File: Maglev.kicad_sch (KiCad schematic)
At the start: 25 parts, among them J1 629722000214, J2 691103110002, J3 61300621121, J4 61300821121, U1 WE-TVS-82400102, U2 ESP32-C3

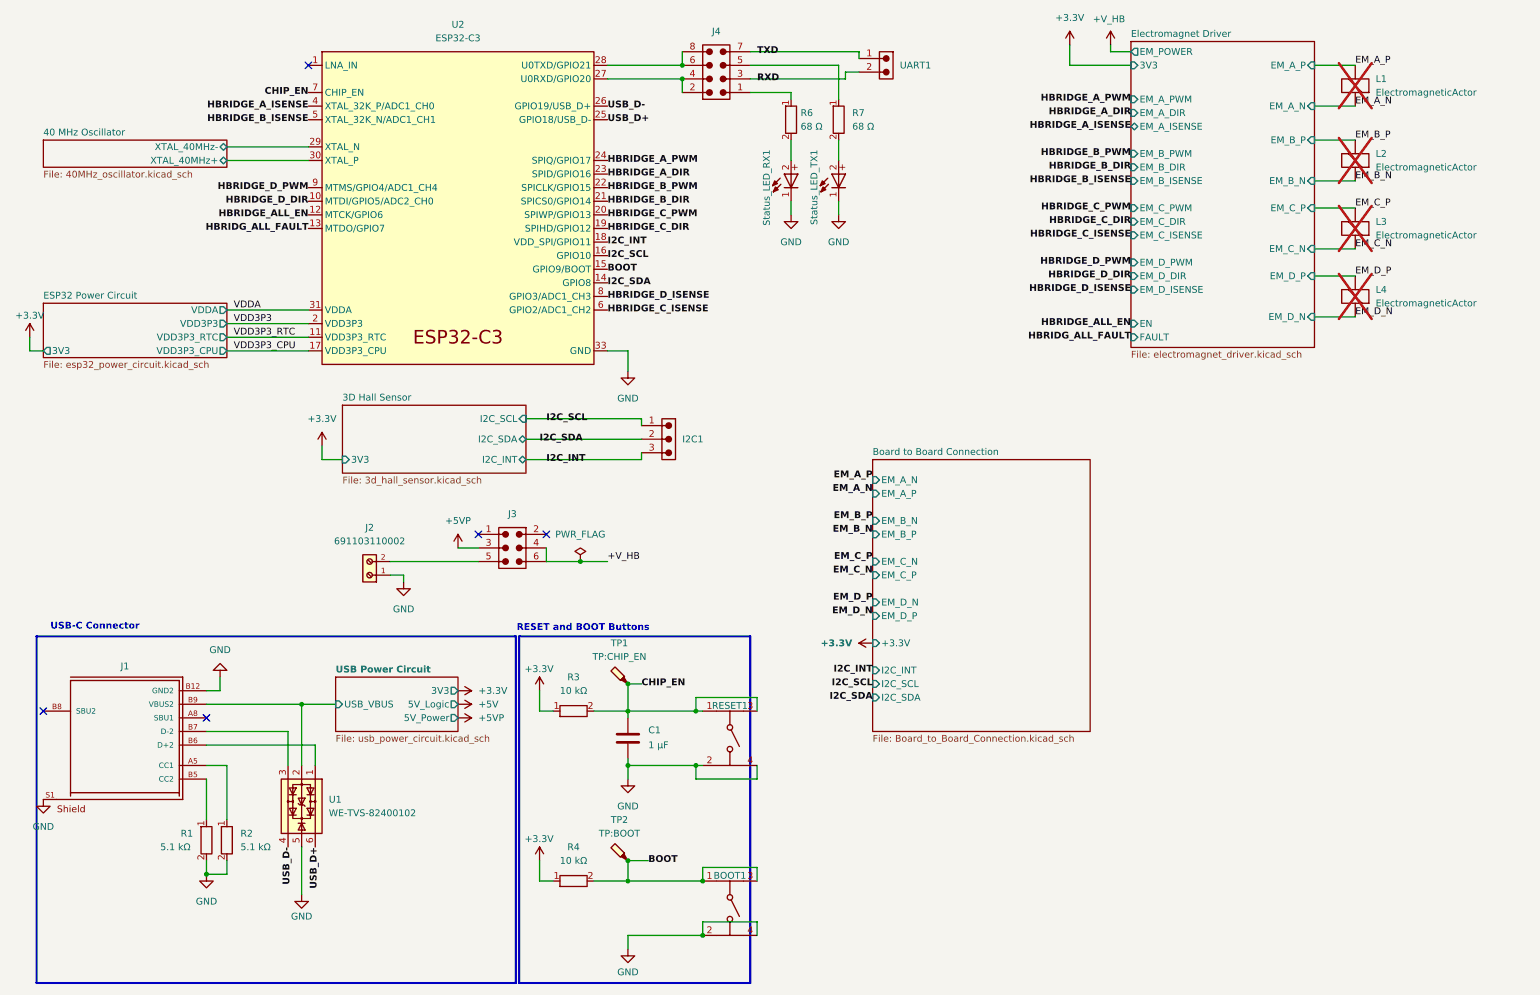
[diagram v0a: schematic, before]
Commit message: Added new ESP32 S3 Module instead of ESP32 C3 in Shematic
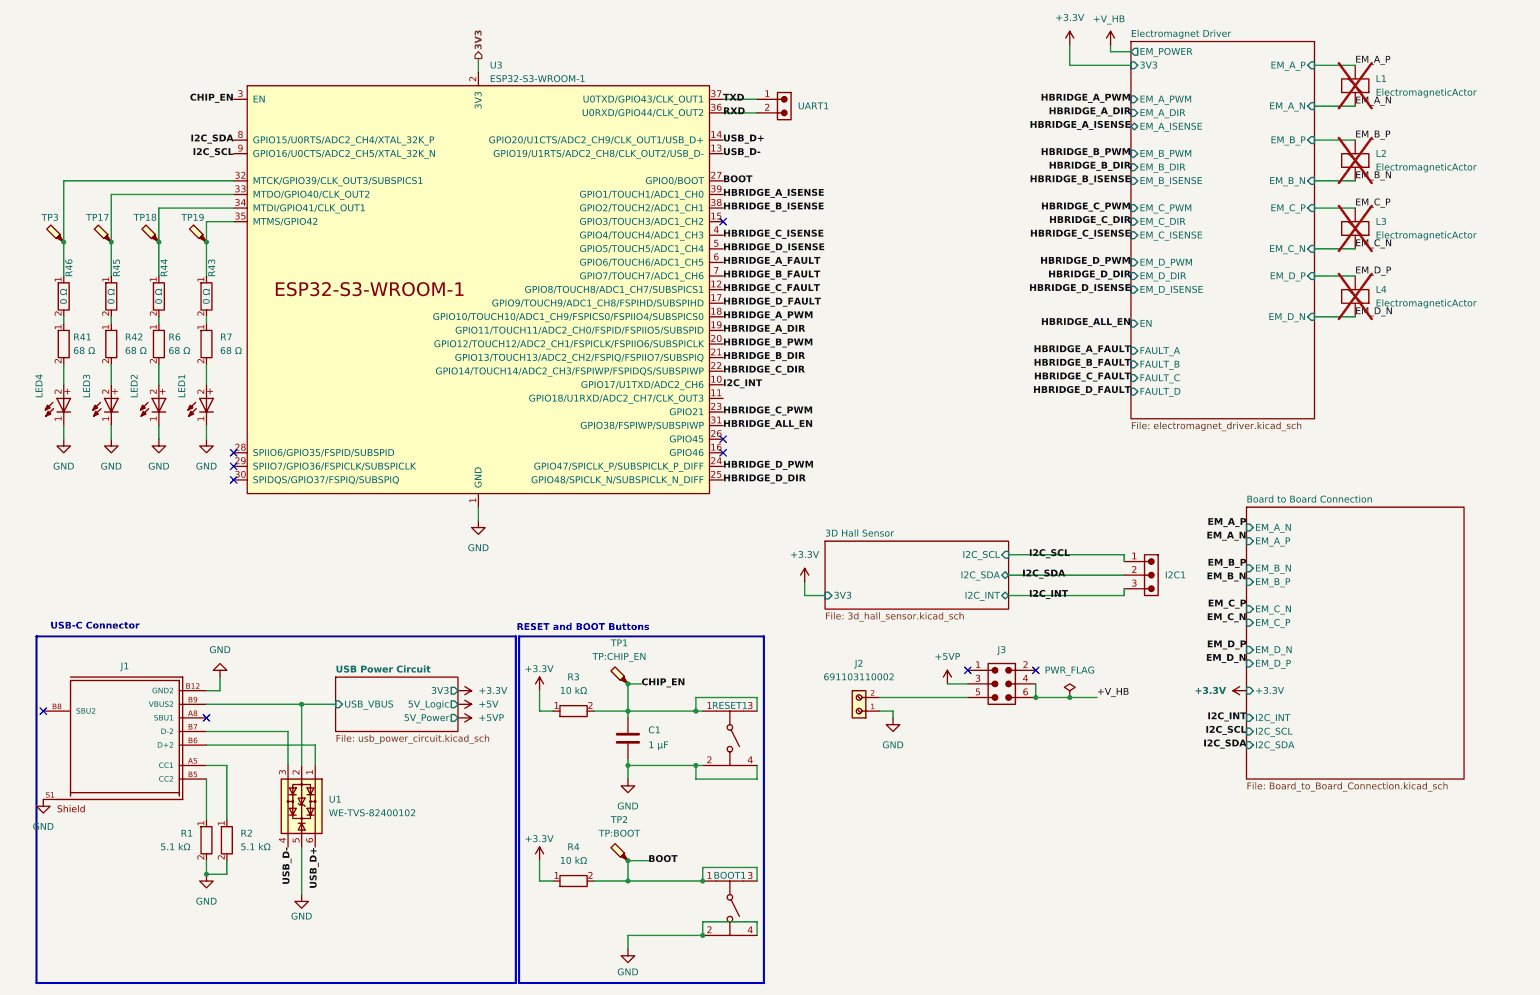
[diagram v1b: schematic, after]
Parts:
- removed J4: 61300821121, Connector_THT_Wurth:J_Wurth_WR-PHD_61300821121, symbol Connector_Wurth_WR-PHD_CUSTOM:61300821121
- removed Status_LED_RX1, Status_LED_TX1: 0603dome_150060VS86000, LED_SMD_Wurth:D_Wurth_WL-SMCW-0603dome, symbol LED_Wurth_WL-SMCW:0603dome_150060VS86000
- removed U2: ESP32-C3, Package_DFN_QFN:QFN-32-1EP_5x5mm_P0.5mm_EP3.45x3.45mm, symbol MCU_Espressif_CUSTOM:ESP32-C3
- added LED1, LED2, LED3, LED4: 0603dome_150060VS86000, LED_SMD_Wurth:D_Wurth_WL-SMCW-0603dome, symbol LED_Wurth_WL-SMCW:0603dome_150060VS86000
- added R41, R42: 1206_R_560112132050, Resistor_SMD_Wurth:R_Wurth_WRIS-RSKS-1206_R, symbol Resistor_Wurth_WRIS-RSKS:1206_R_560112132050
- added R43, R44, R45, R46: 0805_R_560112120002, Resistor_SMD_Wurth:R_Wurth_WRIS-RSKS-0805_R, symbol Resistor_Wurth_WRIS-RSKS:0805_R_560112120002
- added TP17: TP:LED3, symbol Connector:TestPoint_Probe
- added TP18: TP:LED2, symbol Connector:TestPoint_Probe
- added TP19: TP:LED1, symbol Connector:TestPoint_Probe
- added TP3: TP:LED4, symbol Connector:TestPoint_Probe
- added U3: ESP32-S3-WROOM-1, PCM_Espressif:ESP32-S3-WROOM-1U, symbol PCM_Espressif:ESP32-S3-WROOM-1
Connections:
- net BOOT: now also U3.27 (GPIO0/BOOT)
- net CHIP_EN: now also U3.3 (EN)
- net GND: now also LED1.1 (-), LED2.1 (-), LED3.1 (-), LED4.1 (-), U3.1 (GND), U3.40 (GND), U3.41 (GND)
- net HBRIDGE_ALL_EN: now also U3.31 (GPIO38/FSPIWP/SUBSPIWP)
- net HBRIDGE_A_DIR: now also U3.19 (GPIO11/TOUCH11/ADC2_CH0/FSPID/FSPIIO5/SUBSPID)
- net HBRIDGE_A_ISENSE: now also U3.39 (GPIO1/TOUCH1/ADC1_CH0)
- net HBRIDGE_A_PWM: now also U3.18 (GPIO10/TOUCH10/ADC1_CH9/FSPICS0/FSPIIO4/SUBSPICS0)
- net HBRIDGE_B_DIR: now also U3.21 (GPIO13/TOUCH13/ADC2_CH2/FSPIQ/FSPIIO7/SUBSPIQ)
- net HBRIDGE_B_ISENSE: now also U3.38 (GPIO2/TOUCH2/ADC1_CH1)
- net HBRIDGE_B_PWM: now also U3.20 (GPIO12/TOUCH12/ADC2_CH1/FSPICLK/FSPIIO6/SUBSPICLK)
- net HBRIDGE_C_DIR: now also U3.22 (GPIO14/TOUCH14/ADC2_CH3/FSPIWP/FSPIDQS/SUBSPIWP)
- net HBRIDGE_C_ISENSE: now also U3.4 (GPIO4/TOUCH4/ADC1_CH3)
- net HBRIDGE_C_PWM: now also U3.23 (GPIO21)
- net HBRIDGE_D_DIR: now also U3.25 (GPIO48/SPICLK_N/SUBSPICLK_N_DIFF)
- net HBRIDGE_D_ISENSE: now also U3.5 (GPIO5/TOUCH5/ADC1_CH4)
- net HBRIDGE_D_PWM: now also U3.24 (GPIO47/SPICLK_P/SUBSPICLK_P_DIFF)
- net I2C_INT: now also U3.10 (GPIO17/U1TXD/ADC2_CH6)
- net I2C_SCL: now also U3.9 (GPIO16/U0CTS/ADC2_CH5/XTAL_32K_N)
- net I2C_SDA: now also U3.8 (GPIO15/U0RTS/ADC2_CH4/XTAL_32K_P)
- net RXD: now also U3.36 (U0RXD/GPIO44/CLK_OUT2)
- net TXD: now also U3.37 (U0TXD/GPIO43/CLK_OUT1)
- net USB_D+: now also U3.14 (GPIO20/U1CTS/ADC2_CH9/CLK_OUT1/USB_D+)
- net USB_D-: now also U3.13 (GPIO19/U1RTS/ADC2_CH8/CLK_OUT2/USB_D-)
- net at R6.1: now also R44.2
- net at R7.1: now also R43.2
- net at R6.2: now also LED2.2 (+)
- net at R7.2: now also LED1.2 (+)
- new net: R44.1, TP18.1, U3.34 (MTDI/GPIO41/CLK_OUT1)
- new net: R43.1, TP19.1, U3.35 (MTMS/GPIO42)
- new net: R45.1, TP17.1, U3.33 (MTDO/GPIO40/CLK_OUT2)
- new net: R46.1, TP3.1, U3.32 (MTCK/GPIO39/CLK_OUT3/SUBSPICS1)
- new net: R42.1, R45.2
- new net: LED3.2 (+), R42.2
- new net: R41.1, R46.2
- new net: LED4.2 (+), R41.2
- new net 3V3: U3.2 (3V3)
- new net HBRIDGE_A_FAULT: U3.6 (GPIO6/TOUCH6/ADC1_CH5)
- new net HBRIDGE_B_FAULT: U3.7 (GPIO7/TOUCH7/ADC1_CH6)
- new net HBRIDGE_C_FAULT: U3.12 (GPIO8/TOUCH8/ADC1_CH7/SUBSPICS1)
- new net HBRIDGE_D_FAULT: U3.17 (GPIO9/TOUCH9/ADC1_CH8/FSPIHD/SUBSPIHD)
- no-connect marks 5 -> 10
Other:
- removed sheet 40 MHz Oscillator
- removed sheet ESP32 Power Circuit
- sheet Electromagnet Driver ports: added FAULT_A, FAULT_B, FAULT_C, FAULT_D; removed FAULT
- moved on the sheet: I2C1, J2, J3

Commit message: Added JTAG Communication (GPIO3 logic), added capacitors for Vcc, ...
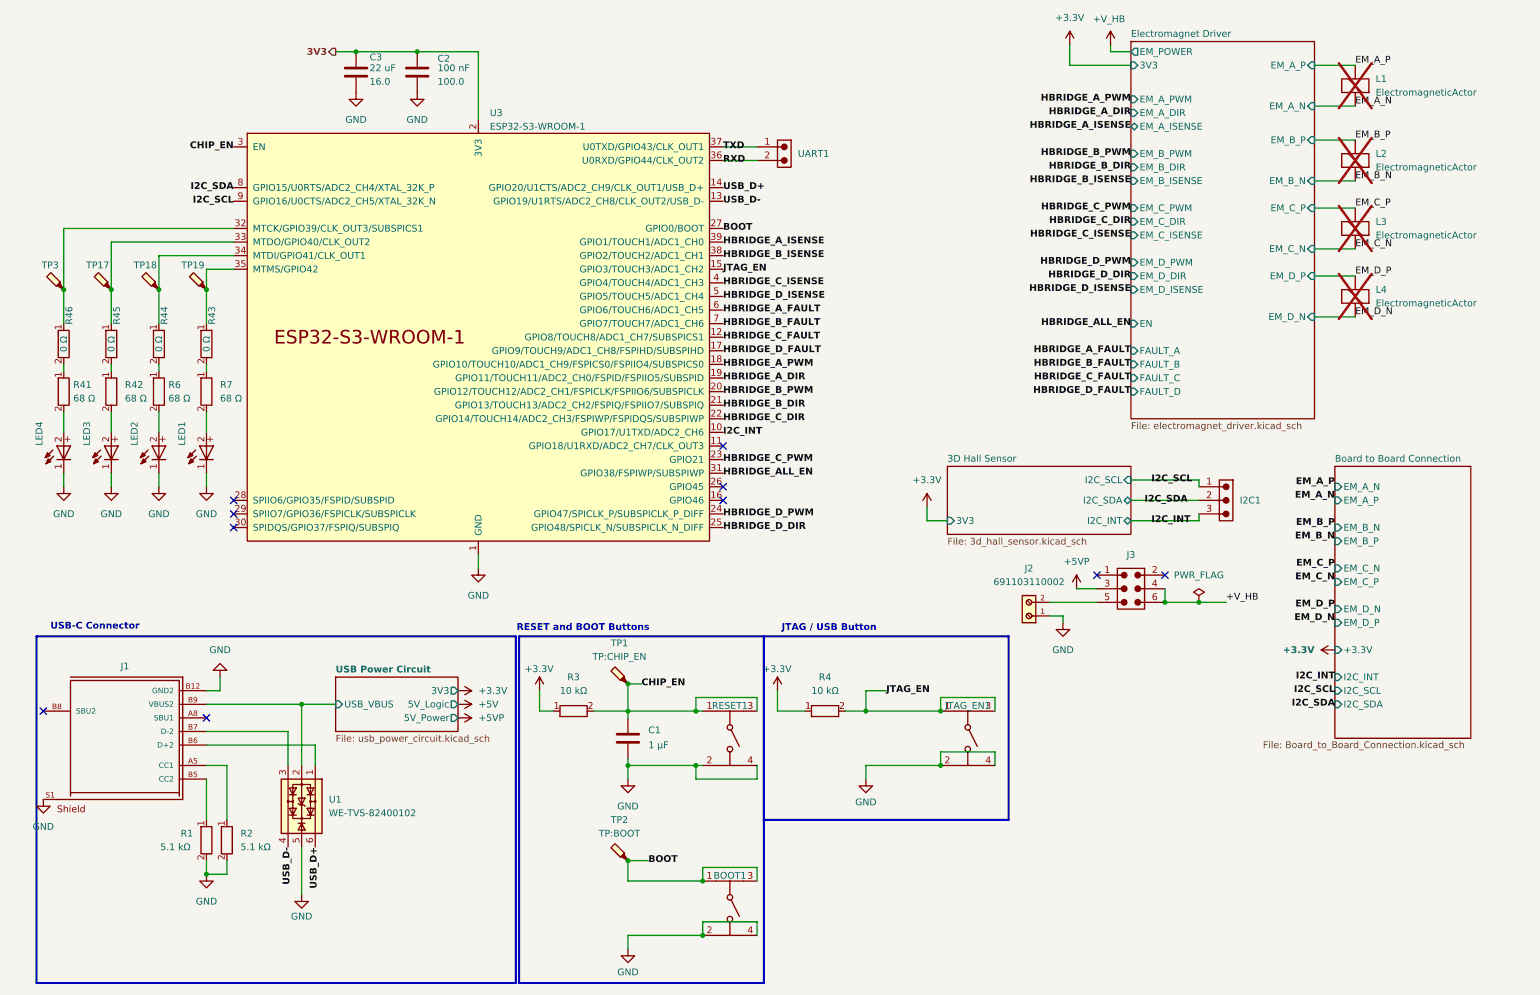
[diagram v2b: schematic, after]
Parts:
- added C2: 100 nF, Capacitor_SMD_Wurth:C_Wurth_WCAP-CSGP-1206_H1.25, symbol Capacitor_Wurth_WCAP-CSGP:1206_H1.25_885012208118
- added C3: 22 uF, Capacitor_SMD_Wurth:C_Wurth_WCAP-CSGP-1206_H1.6, symbol Capacitor_Wurth_WCAP-CSGP:1206_H1.6_885012108018
- added JTAG_EN1: 430182043816, Switch_SMD_Wurth:SW_Wurth_WS-TASV_430182043816, symbol Switch_Wurth_WS-TASV:430182043816
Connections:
- net 3V3: now also C2.1, C3.1
- net BOOT: no longer R4.2
- net GND: now also C2.2, C3.2, JTAG_EN1.2, JTAG_EN1.4
- net JTAG_EN: now reaches U3.15 (GPIO3/TOUCH3/ADC1_CH2)
- net JTAG_EN: now also R4.2, JTAG_EN1.1, JTAG_EN1.3
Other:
- note added: "JTAG / USB Button"
- moved on the sheet: I2C1, J2, J3, LED1, LED2, LED3, LED4, R41, R42, R43, R44, R45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

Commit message: continued and finished conversion to ESP32-S3-WROOM module
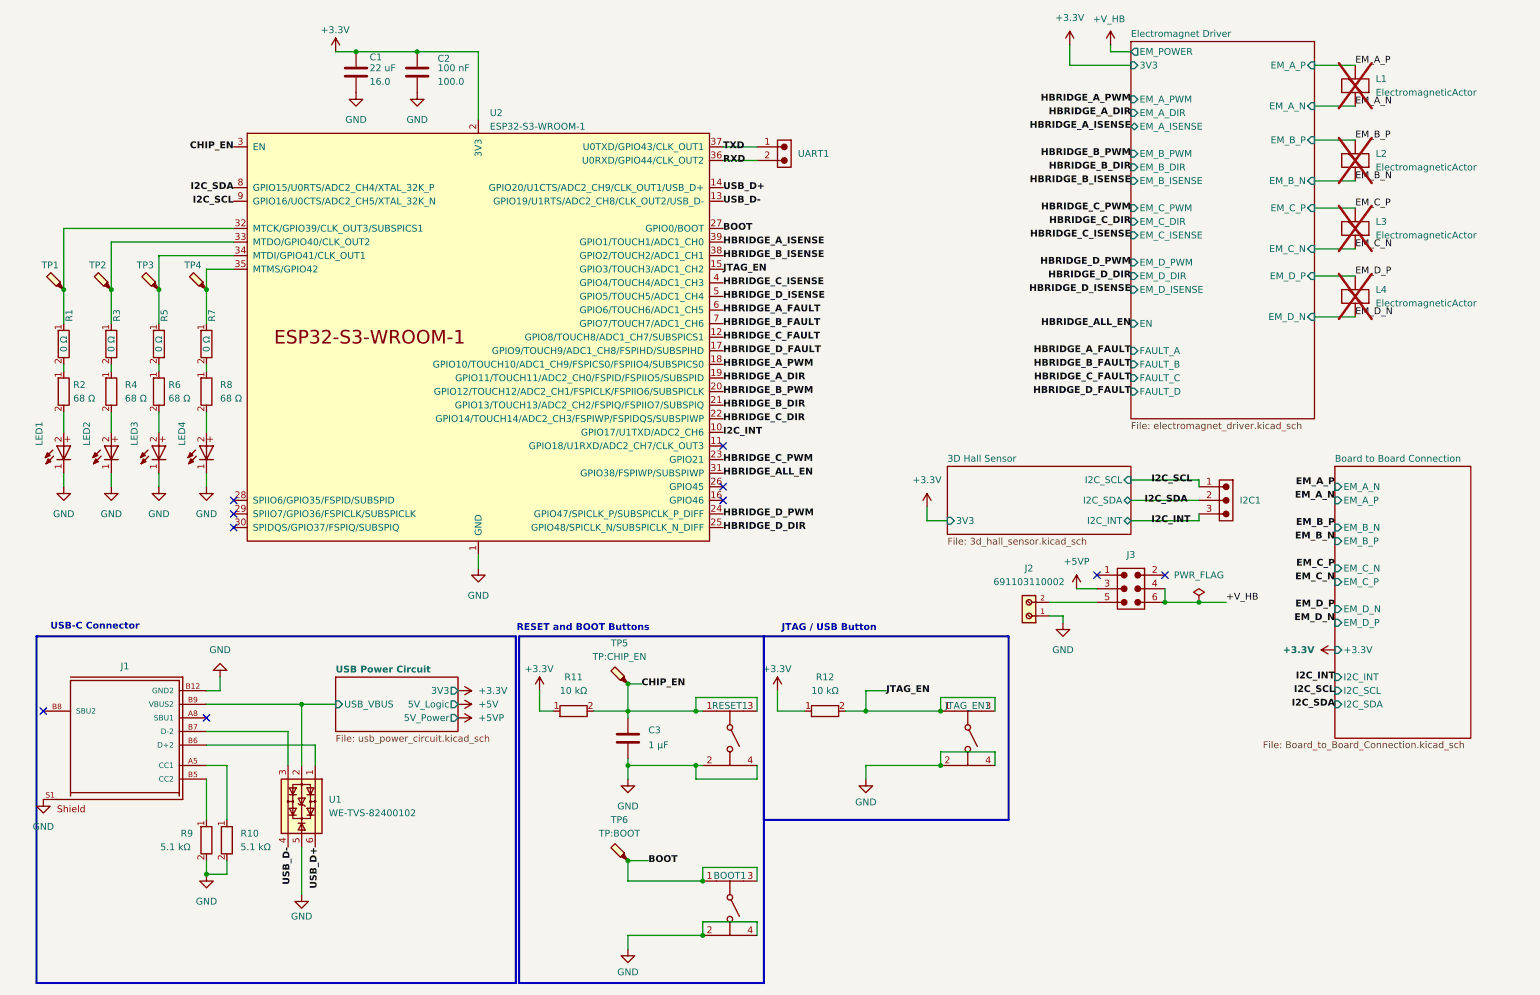
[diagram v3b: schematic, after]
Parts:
- TP1: renamed from TP3; footprint (none) -> TestPoint:TestPoint_Pad_D2.0mm
- TP2: renamed from TP17; footprint (none) -> TestPoint:TestPoint_Pad_D2.0mm
- TP3: renamed from TP18; footprint (none) -> TestPoint:TestPoint_Pad_D2.0mm
- TP4: renamed from TP19; footprint (none) -> TestPoint:TestPoint_Pad_D2.0mm
- renumbered C3 to C1, C1 to C3, LED4 to LED1, LED3 to LED2, LED2 to LED3, LED1 to LED4, R46 to R1, R2 to R10, R3 to R11, R4 to R12, R41 to R2, R45 to R3, R42 to R4, R44 to R5, R43 to R7, R7 to R8, R1 to R9, TP1 to TP5, TP2 to TP6, U3 to U2
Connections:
- net 3V3 is gone; now on net +3.3V: C1.1, C2.1, U2.2 (3V3)
